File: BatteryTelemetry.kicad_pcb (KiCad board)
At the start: 2 copper layers, 137 parts, among them IC1 BQ76925PWR, IC2 BQ76925PWR, IC3 BQ76925PWR, IC4 BQ76925PWR, J1 Conn_01x07_Pin, J2 Conn_01x07_Pin, J3 Conn_01x07_Pin, J4 Conn_01x07_Pin, J5 USB_C_Receptacle_USB2.0, J6 Conn_01x04_Socket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

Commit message: footprint v1 (unfinished)
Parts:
- moved C37 89.4 mm to (93.5, 31.1), turned to 90 degrees
- moved R23 82.2 mm to (69.3, 106.8), turned to 90 degrees
- moved R24 80.1 mm to (72.3, 106.8), turned to 90 degrees
- moved R25 78.1 mm to (75.2, 106.8), turned to 90 degrees
- moved R26 76.4 mm to (78.2, 106.8), turned to 90 degrees
- moved R27 74.8 mm to (81.1, 106.8), turned to 90 degrees
- moved Y1 74.5 mm to (87.4, 57.6)
- moved R28 73.4 mm to (84.1, 106.8), turned to 90 degrees
- moved H1 73.2 mm to (96.3, 96.0)
- moved IC3 72.8 mm to (45.3, 92.6), turned to 90 degrees
- moved IC4 72.4 mm to (73.3, 93.4), turned to 90 degrees
- moved R15 71.8 mm to (37.8, 106.8), turned to 90 degrees
- moved H2 69.8 mm to (104.0, 96.0)
- moved J4 69.6 mm to (67.2, 113.9)
- moved R16 68.6 mm to (40.7, 106.8), turned to 90 degrees
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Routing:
- net +3V3: track 0.00 -> 136.7 mm, vias 0 -> 4
- net /SCL_BAT1: track 0.00 -> 42.0 mm
- net /SDA_BAT1: track 0.00 -> 39.5 mm
- net /BAT3: track 0.00 -> 38.4 mm, vias 0 -> 2
- net /BAT1: track 0.00 -> 37.5 mm, vias 0 -> 2
- net /SCL_BAT3: track 0.00 -> 35.1 mm
- net /V3_BAT: track 0.00 -> 33.0 mm
- net Net-(U1-USB_DM): track 0.00 -> 32.2 mm, vias 0 -> 2
- net Net-(U1-USB_DP): track 0.00 -> 31.1 mm, vias 0 -> 2
- net /SDA_BAT3: track 0.00 -> 29.5 mm
- net Net-(D1-K): track 0.00 -> 25.5 mm
- net /BAT4: track 0.00 -> 24.8 mm, vias 0 -> 2
- net /SCL_BAT2: track 0.00 -> 22.5 mm
- net /QSPI_CS: track 0.00 -> 21.0 mm
- net /SCL_BAT4: track 0.00 -> 18.0 mm
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
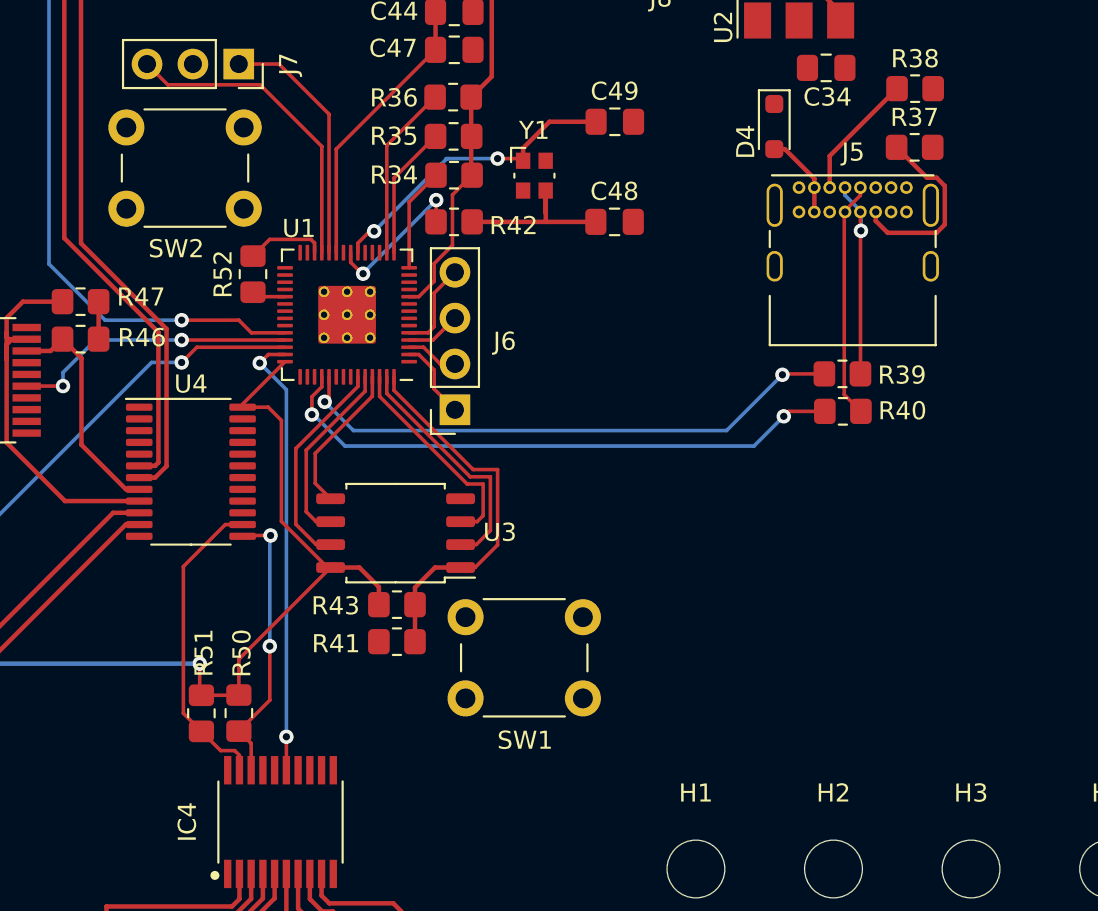
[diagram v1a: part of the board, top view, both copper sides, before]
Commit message: button fixed
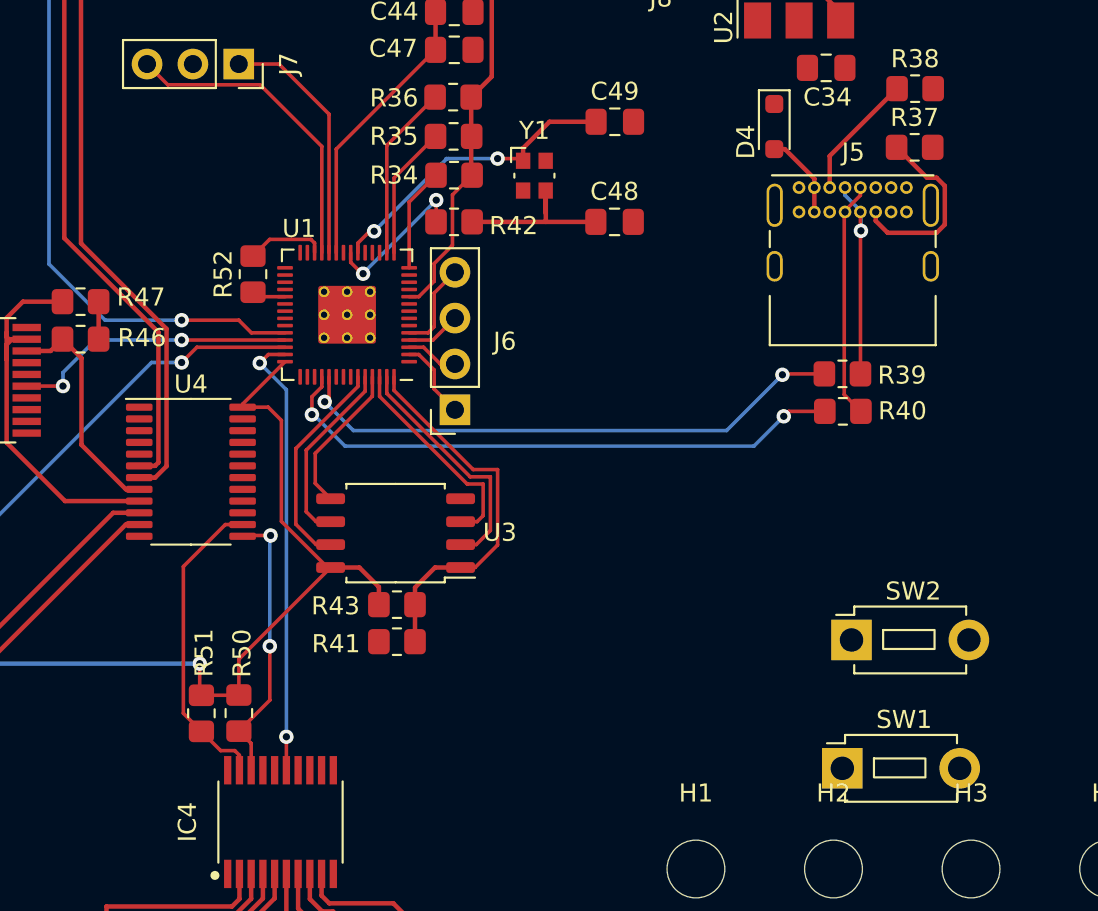
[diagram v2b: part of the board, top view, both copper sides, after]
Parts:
- SW1, SW2: value SW_MEC_5G -> SW_Push; footprint Button_Switch_THT:SW_PUSH_6mm_H4.3mm -> Button_Switch_THT:SW_PUSH_1P1T_6x3.5mm_H4.3_APEM_MJTP1243
- moved SW2 49.2 mm to (105.0, 83.3)
- moved SW1 14.9 mm to (104.4, 90.4), turned to 0 degrees
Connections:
- R41 pad 1: /~{USB_BOOT} -> /USB_BOOT
- SW1 pad 1: GND -> /USB_BOOT
- SW2 pad 1: GND -> /RUN

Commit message: finished layout
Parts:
- moved H3 109.1 mm to (31.8, 21.6)
- moved H4 93.7 mm to (62.2, 21.6)
- moved H1 78.9 mm to (31.6, 141.0)
- moved J8 78.7 mm to (74.9, 116.5)
- moved J7 74.0 mm to (74.9, 125.3), turned to 0 degrees
- moved J6 71.7 mm to (74.9, 141.8)
- moved H2 62.2 mm to (61.0, 141.0)
- moved SW2 60.4 mm to (65.8, 129.3), turned to -90 degrees
- moved SW1 57.9 mm to (61.6, 129.3), turned to -90 degrees
- moved R37 50.4 mm to (65.2, 30.2), turned to -90 degrees
- moved R40 50.2 mm to (69.5, 34.8), turned to 90 degrees
- moved R28 49.9 mm to (43.4, 135.8), turned to 0 degrees
- moved C28 49.3 mm to (48.1, 135.8), turned to 0 degrees
- moved R39 47.2 mm to (71.5, 34.8), turned to -90 degrees
- moved R27 45.8 mm to (43.4, 132.8), turned to 0 degrees
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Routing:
- net GND: track 0.00 -> 74.9 mm, vias 0 -> 31
- net /V3_EXT: track 10.3 -> 82.2 mm
- net /V5_EXT: track 6.13 -> 64.8 mm, vias 0 -> 1
- net /RUN: track 4.41 -> 59.7 mm, vias 0 -> 1
- net /UART0 TX: track 4.43 -> 59.7 mm, vias 0 -> 3
- net /UART0 RX: track 2.92 -> 57.4 mm, vias 0 -> 3
- net /UART0 CTS: track 3.04 -> 55.7 mm, vias 0 -> 3
- net /SDA_BAT1: track 39.5 -> 91.5 mm, vias 0 -> 2
- net /UART0 RTS: track 5.02 -> 53.6 mm, vias 0 -> 3
- net /SCL_BAT1: track 42.0 -> 87.8 mm
- net /I2C0 SDA: track 7.40 -> 51.1 mm, vias 0 -> 2
- net /SDA_BAT2: track 12.8 -> 55.5 mm
- net Net-(J7-Pin_1): track 13.8 -> 54.4 mm, vias 0 -> 3
- net /SCL_BAT2: track 22.5 -> 62.2 mm
- net Net-(J7-Pin_3): track 17.5 -> 56.7 mm, vias 0 -> 3
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- added copper zone on B.Cu, net GND
- added copper zone on F.Cu, net GND
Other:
- board outline added: 50.8 x 127 mm
- board text added: "Power Switch V3_BAT/V3_EXT"
- board text added: "Reset RUN"
- board text added: "Reset USB_BOOT"
